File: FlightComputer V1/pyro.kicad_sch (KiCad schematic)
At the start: 0 parts

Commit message: add pyro
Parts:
- added J?: Screw_Terminal_01x02, symbol Connector:Screw_Terminal_01x02
- added Q3: NMOS, symbol Simulation_SPICE:NMOS
- added Q?: PMOS, symbol Simulation_SPICE:PMOS
- added R1, R3, R4, R?: R_Small, symbol Device:R_Small
- added R2, R?: R, symbol Device:R
- added R?: Heater, symbol Device:Heater
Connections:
- new net: J?.1 (Pin_1), Q?.3 (S)
- new net: Q3.2 (G), R1.1
- new net: Q3.1 (D), R?.1, R?.1
- new net: Q?.2 (G), R?.2
- new net +BATT: J?.2 (Pin_2), Q?.1 (D), R3.1, R?.1, R?.2
- new net GNDPWR: Q3.3 (S), R2.1, R4.2, R?.2
- new net cont_out: R3.2, R4.1
- new net pyro_in: R1.2, R2.2

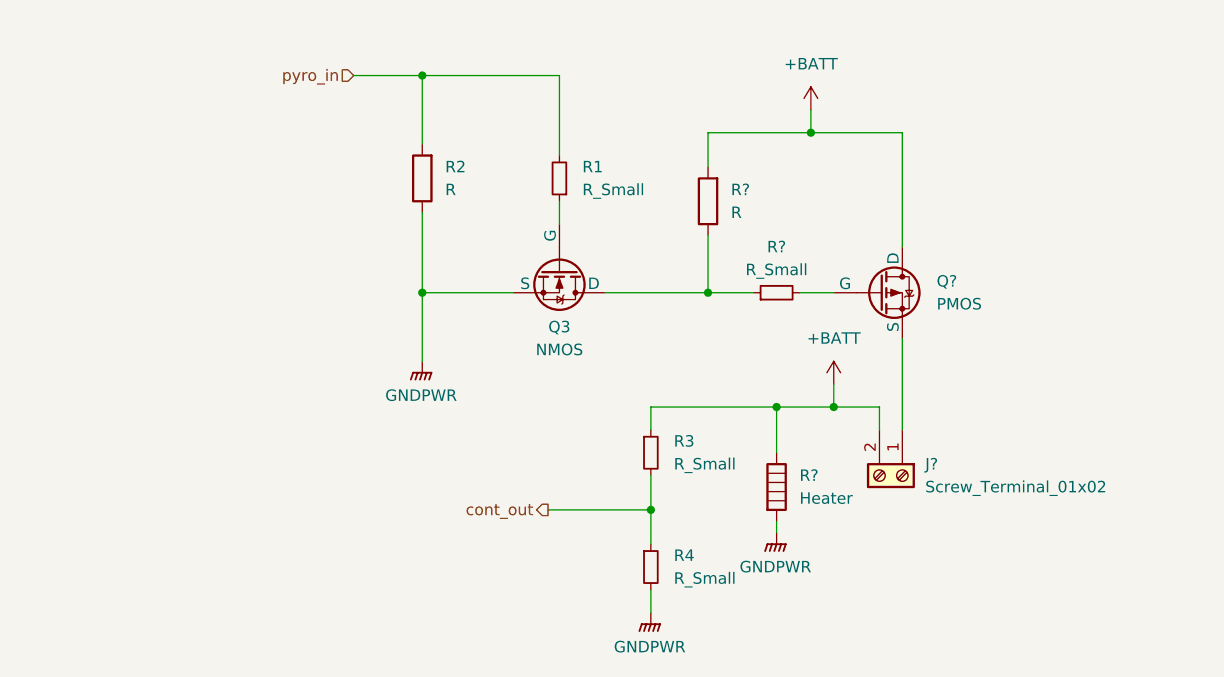
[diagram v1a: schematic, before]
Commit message: Rework pyro channel sheet
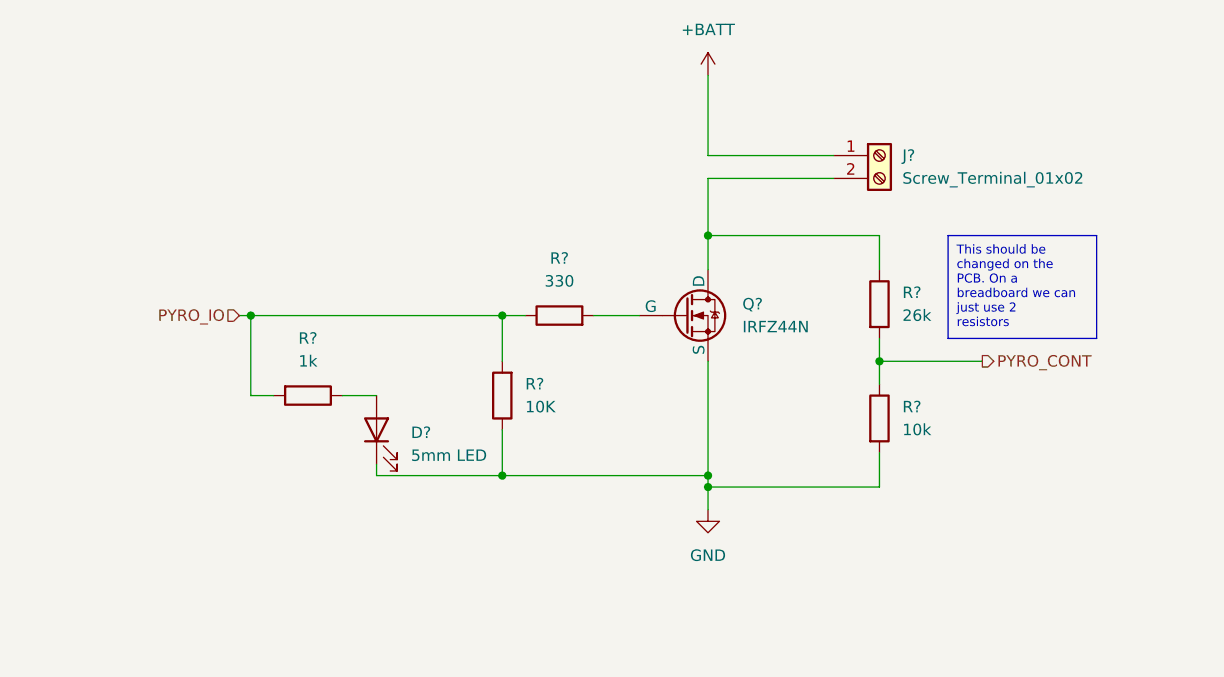
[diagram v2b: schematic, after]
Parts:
- removed J?: Screw_Terminal_01x02, symbol Connector:Screw_Terminal_01x02
- removed Q3: NMOS, symbol Simulation_SPICE:NMOS
- removed Q?: PMOS, symbol Simulation_SPICE:PMOS
- removed R1, R3, R4, R?: R_Small, symbol Device:R_Small
- removed R2, R?: R, symbol Device:R
- removed R?: Heater, symbol Device:Heater
- added D?: 5mm LED, symbol Device:LED
- added J?: Screw_Terminal_01x02, symbol Connector:Screw_Terminal_01x02
- added Q?: IRFZ44N, symbol Simulation_SPICE:NMOS
- added R?: 26k, symbol Device:R
- added R?: 1k, symbol Device:R
- added R?: 10k, symbol Device:R
- added R?: 10K, symbol Device:R
- added R?: 330, symbol Device:R
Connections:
- net +BATT: now also J?.1 (Pin_1)
- new net: J?.2 (Pin_2), Q?.1 (D), R?.1
- new net: D?.2 (A), R?.1
- new net: Q?.2 (G), R?.2
- new net GND: D?.1 (K), Q?.3 (S), R?.1, R?.2
- new net PYRO_CONT: R?.1, R?.2
- new net PYRO_IO: R?.1, R?.2, R?.2

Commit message: Update pyro channel. Duplicate sheet. Paramatarize labels
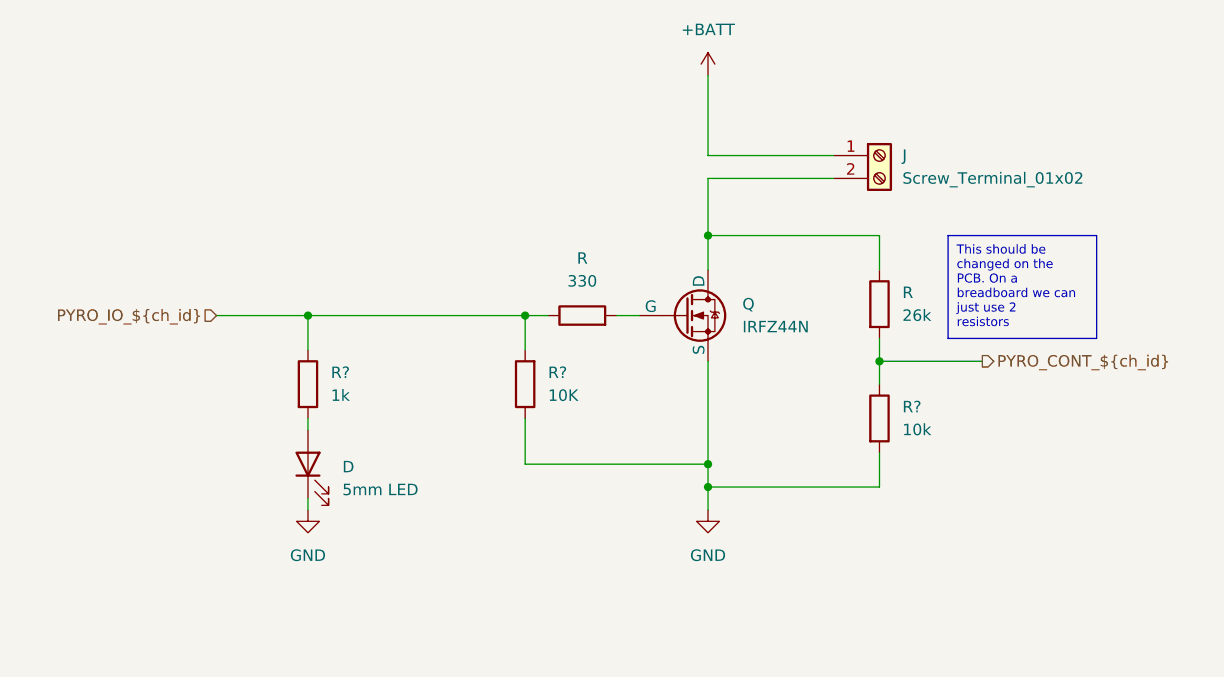
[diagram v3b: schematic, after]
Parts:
- gave numbers to parts that had none: 4
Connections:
- net at D.2 (A): now also R?.2; no longer R?.1
- net PYRO_CONT renamed PYRO_CONT_${ch_id}
- net PYRO_IO renamed PYRO_IO_${ch_id}
- net PYRO_IO_${ch_id}: now also R?.1; no longer R?.2
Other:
- moved on the sheet: D, R, R?
